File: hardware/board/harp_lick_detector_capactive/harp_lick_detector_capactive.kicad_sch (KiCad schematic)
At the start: 45 parts

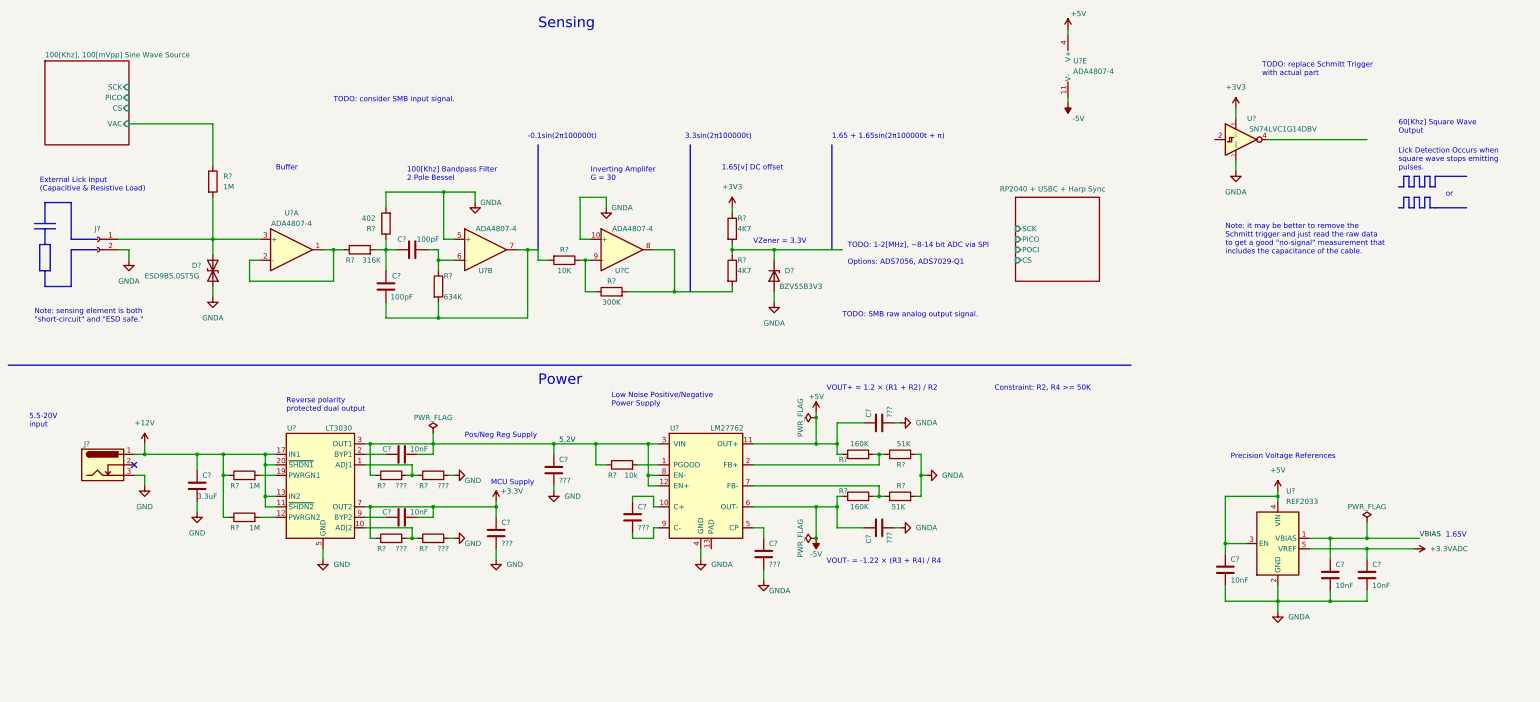
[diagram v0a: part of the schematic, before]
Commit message: add pico-sdk; draft as9833 driver
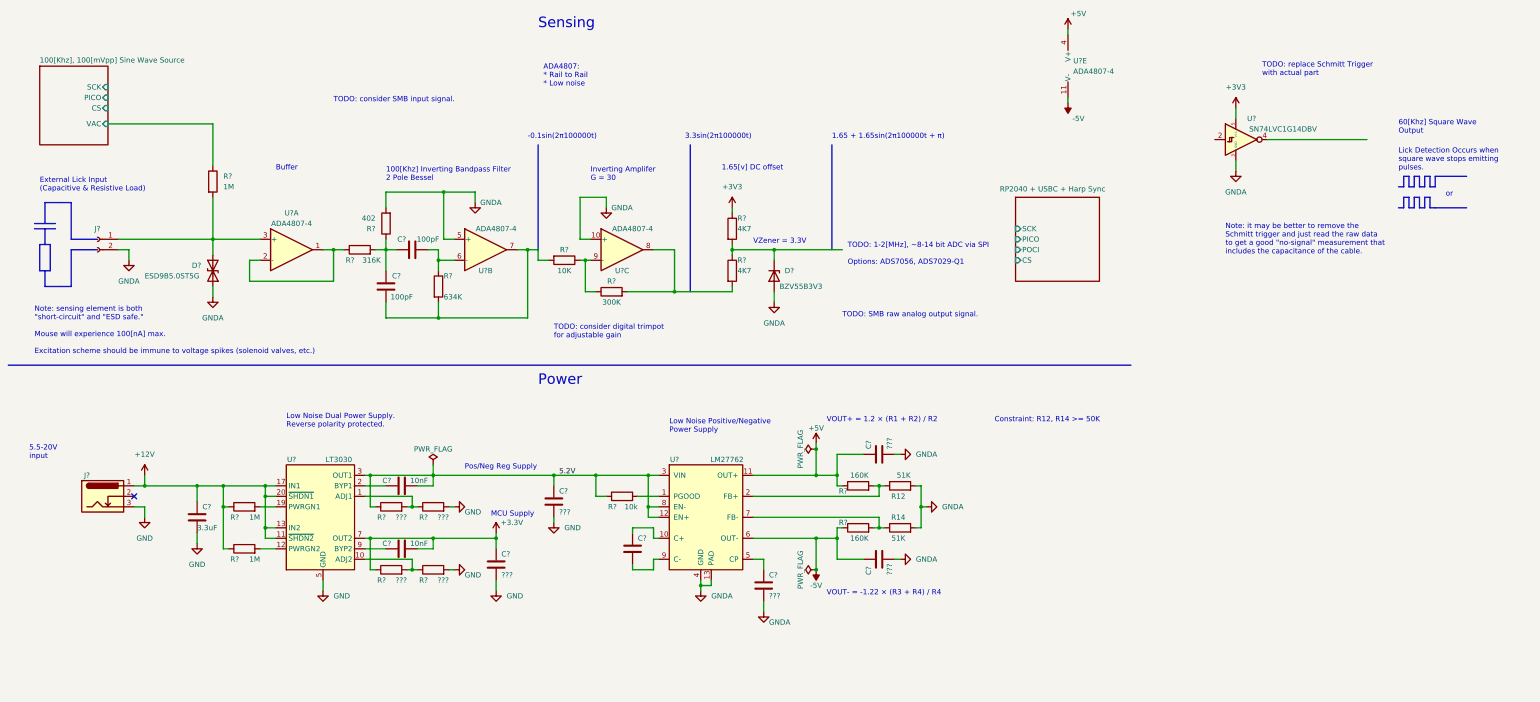
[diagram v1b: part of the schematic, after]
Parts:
- removed C? (x3): 10nF, symbol Device:C
- removed U?: REF2033, Package_TO_SOT_SMD:SOT-23-5, symbol machine_agency_components:REF20xx
- C?: value ??? -> (none)
- gave numbers to parts that had none: 2
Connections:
- net GNDA: now also U?.13 (PAD)
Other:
- note added: "100[Khz] Inverting Bandpass Filter 2 Pole Bessel"
- note added: "ADA4807: * Rail to Rail * Low noise"
- note added: "Constraint: R12, R14 >= 50K"
- note added: "Low Noise Dual Power Supply. Reverse polarity protected."
- note added: "Note: sensing element is both "short-circuit" and "ESD safe." Mouse will experience 100[nA] max. Excitation scheme should be immune to voltage spikes (solenoid valves, etc.)"
- note added: "TODO: consider digital trimpot for adjustable gain"
- note removed: "1.65V"
- note removed: "100[Khz] Bandpass Filter 2 Pole Bessel"
- note removed: "Constraint: R2, R4 >= 50K"
- note removed: "Note: sensing element is both "short-circuit" and "ESD safe.""
- note removed: "Precision Voltage References"
- note removed: "Reverse polarity protected dual output"
- moved on the sheet: C?, J?, R12, R14, R?, U?

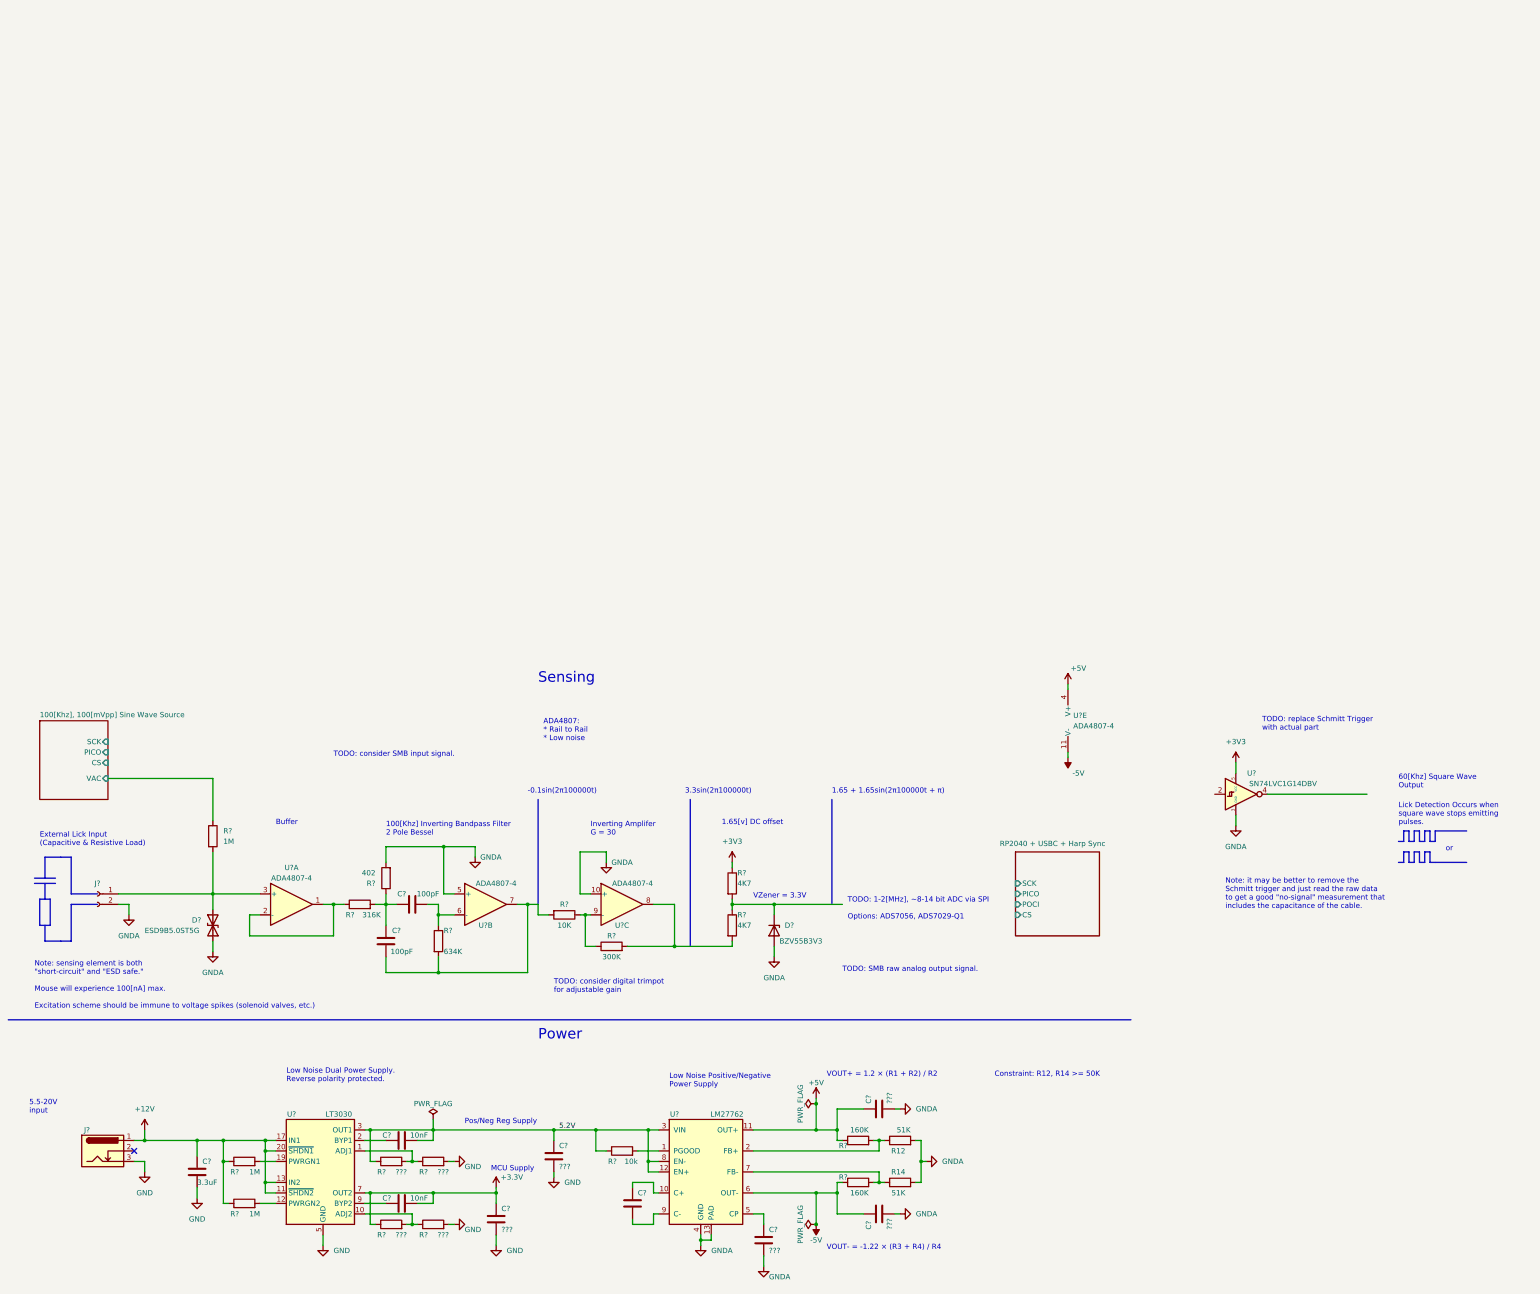
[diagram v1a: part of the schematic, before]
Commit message: update schematic
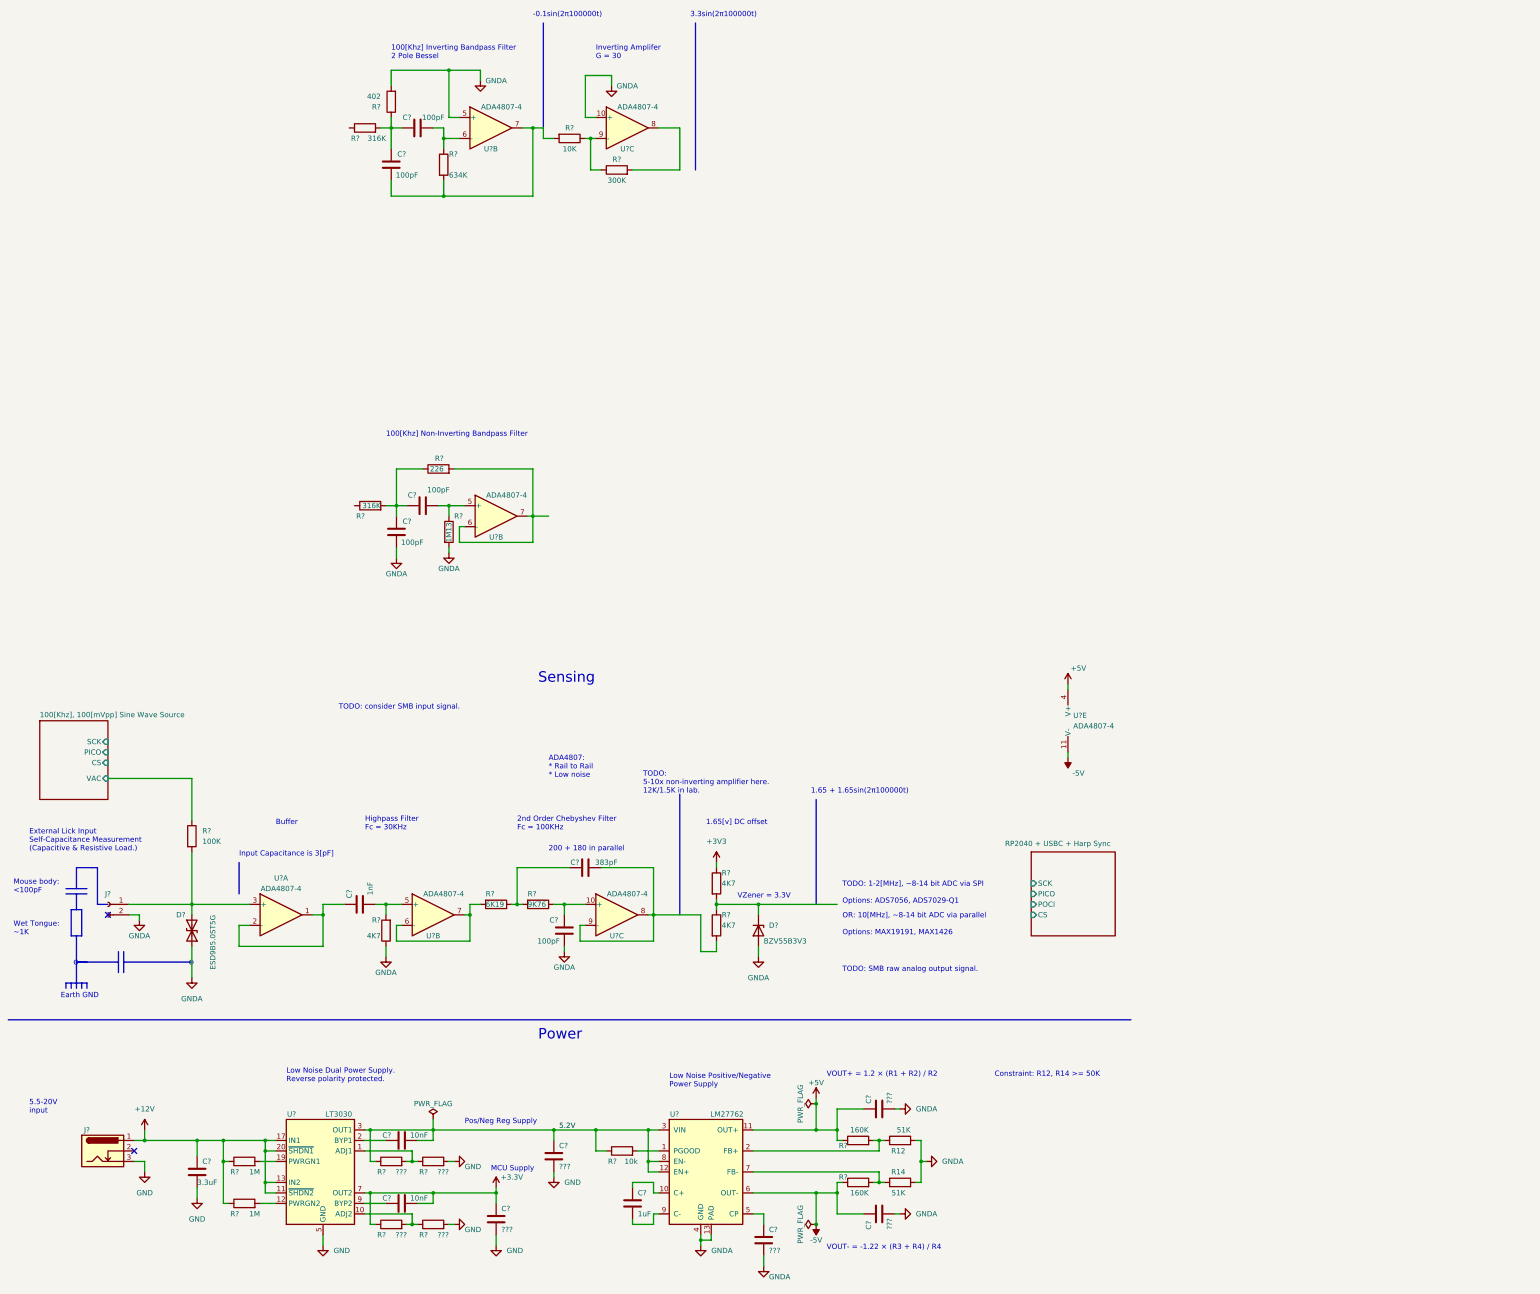
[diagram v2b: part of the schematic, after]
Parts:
- removed U?: SN74LVC1G14DBV, Package_TO_SOT_SMD:SOT-23-5, symbol 74xGxx:SN74LVC1G14DBV
- added C? (x3): 100pF, symbol Device:C
- added C?: 383pF, symbol Device:C
- added C?: 1nF, symbol Device:C
- added R?: 1M13, symbol Device:R
- added R?: 4K7, symbol Device:R
- added R?: 9K76, symbol Device:R
- added R?: 226, symbol Device:R
- added R?: 316K, symbol Device:R
- added R?: 6K19, symbol Device:R
- added U? (x3): ADA4807-4, symbol Amplifier_Operational:ADA4807-4
- C?: value (none) -> 1uF
- R?: value 1M -> 100K
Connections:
- net GNDA: now also C?.2, C?.2, R?.1, R?.2
- net at R?.2, U?.8: no longer R?.2
- net at U?.1, U?.2 (-): now also C?.1; no longer R?.1
- new net: C?.2, R?.1, U?.5 (+)
- new net: C?.2, R?.2, U?.5 (+)
- new net: R?.2, U?.6 (-), U?.7 (x2)
- new net: C?.1, R?.1, U?.10 (+)
- new net: C?.1, R?.2, U?.8, U?.9 (-)
- new net: C?.1, C?.1, R?.1, R?.2
- new net: C?.2, R?.1, R?.2
- no-connect marks 1 -> 2
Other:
- note added: "1.65 + 1.65sin(2π100000t)"
- note added: "100[Khz] Non-Inverting Bandpass Filter"
- note added: "200 + 180 in parallel"
- note added: "2nd Order Chebyshev Filter Fc = 100KHz"
- note added: "Earth GND"
- note added: "External Lick Input Self-Capacitance Measurement (Capacitive & Resistive Load.)"
- note added: "Highpass Filter Fc = 30KHz"
- note added: "Input Capacitance is 3[pF]"
- note added: "Mouse body: <100pF"
- note added: "OR: 10[MHz], ~8-14 bit ADC via parallel Options: MAX19191, MAX1426"
- note added: "TODO: 5-10x non-inverting amplifier here. 12K/1.5K in lab."
- note added: "Wet Tongue: ~1K"
- note added: "o"
- note removed: "1.65 + 1.65sin(2π100000t + π)"
- note removed: "60[Khz] Square Wave Output"
- note removed: "External Lick Input (Capacitive & Resistive Load)"
- note removed: "Lick Detection Occurs when square wave stops emitting pulses."
- note removed: "Note: it may be better to remove the Schmitt trigger and just read the raw data to get a good "no-signal" measurement that includes the capacitance of the cable."
- note removed: "Note: sensing element is both "short-circuit" and "ESD safe." Mouse will experience 100[nA] max. Excitation scheme should be immune to voltage spikes (solenoid valves, etc.)"
- note removed: "TODO: consider digital trimpot for adjustable gain"
- note removed: "TODO: replace Schmitt Trigger with actual part"
- note removed: "or"
- moved on the sheet: C?, D?, J?, R?, U?A, U?B, U?C
